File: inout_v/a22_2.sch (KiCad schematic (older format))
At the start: 38 parts, among them U2062 74HC02, U22028 74LVC07, U22029 74HC02, U22030 74HC27, U22032 74HC02, U22033 74HC27, U22034 74HC02, U22035 74HC4002, U22036 74HC02, U22037 74HC27, U22038 74HC02, U22039 74HC02, U22040 74HC02, U22041 74HC27, U22042 74HC02, U22043 74HC02, U22044 74HC27, U22045 74HC02, U22046 74HC4002, U22047 74HC02, U22048 74HC27, U22049 74HC02, U22050 74HC02, U22051 74HC27, U22052 74HC02, U22053 74HC02, U22054 74HC02, U22055 74HC27, U22056 74HC4002, U22057 74LVC07, U22058 74HC02, U22059 74HC02, U22060 74HC27, U22061 74HC02, U22062 74HC02, U22063 74HC27, U22064 74HC02, U22065 74HC02

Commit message: Added and tied in Inout VI. Pulled in all PIPA related things. Almost there!
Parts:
- added unit 3 of U22057
- added unit 2 of U22065
- added unit 3 of U22065
- added unit 4 of U22065
- added U22066: 74HC27, symbol 74HC27
- added U22067: 74HC02, symbol 74HC02
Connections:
- net CCH35: now also U22065.12, U22067.9
- net CHWL01/: now also U22065.6
- net DATA/: now also U22057.6
- net GND: now also U22057.7 (GND), U22065.7 (GND), U22065.7 (GND), U22065.7 (GND), U22066.7 (GND), U22066.7 (GND), U22067.7 (GND), U22067.7 (GND), U22067.7 (GND), U22067.7 (GND)
- net HIGH3/: now also U22066.1, U22066.3
- net LOW6/: now also U22066.13
- net LOW7/: now also U22066.5
- net PC15/: now also U22067.3
- net VCC: now also U22057.14 (VCC), U22065.14 (VCC), U22065.14 (VCC), U22065.14 (VCC), U22066.14 (VCC), U22066.14 (VCC), U22067.14 (VCC), U22067.14 (VCC), U22067.14 (VCC), U22067.14 (VCC)
- net WCH35/: now also U22065.5, U22067.2
- new net: U22065.4, U22065.8
- new net: U22065.10, U22065.11, U22066.2
- new net: U22065.13, U22065.9
- new net: U22066.12, U22067.11
- new net: U22067.1, U22067.5
- new net: U22066.4, U22067.4, U22067.8
- new net: U22067.10, U22067.6
- new net: U22066.6, U22067.12
- new net: U22057.5, U22067.13
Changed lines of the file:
@@
 Connection ~ 14650 1800
 Wire Wire Line
-	12850 2750 12850 18350
+	12850 2750 12850 20750
 Connection ~ 12850 2750
 Wire Wire Line
-	11550 1750 11550 17350
+	11550 1750 11550 19750
 Wire Wire Line
 	11550 2950 11600 2950
@@
 $EndComp
 Wire Wire Line
-	18300 3200 18300 12800
+	18300 3200 18300 18850
 $Comp
 L 74HC02 U22058
@@
 	14650 1800 14650 10200
 Wire Wire Line
-	14650 11400 14650 17400
+	14650 11400 14650 19800
 Wire Wire Line
 	18300 8000 18500 8000
@@
 Text HLabel 14600 11400 0    60   Input ~ 0
 HIGH3/
+Wire Wire Line
+	15900 18750 16200 18750
+Wire Wire Line
+	15900 19950 16100 19950
+$Comp
+L 74HC02 U22065
+U 2 1 574071CE
+P 12200 18650
+F 0 "U22065" H 12200 18700 60  0000 C CNN
+F 1 "74HC02" H 12250 18600 60  0000 C CNN
+F 2 "" H 12200 18650 60  0000 C CNN
+F 3 "" H 12200 18650 60  0000 C CNN
+	2    12200 18650
+	1    0    0    -1
+$EndComp
+$Comp
+L 74HC02 U22065
+U 3 1 574071D5
+P 13550 18750
+F 0 "U22065" H 13550 18800 60  0000 C CNN
+F 1 "74HC02" H 13600 18700 60  0000 C CNN
+F 2 "" H 13550 18750 60  0000 C CNN
+F 3 "" H 13550 18750 60  0000 C CNN
+F 4 "1" H 13800 18750 60  0000 C CIN "Initial"
+	3    13550 18750
+	1    0    0    -1
+$EndComp
+Wire Wire Line
+	12800 18650 12950 18650
+$Comp
+L 74HC02 U22065
+U 4 1 574071DC
+P 13550 19450
+F 0 "U22065" H 13550 19500 60  0000 C CNN
+F 1 "74HC02" H 13600 19400 60  0000 C CNN
+F 2 "" H 13550 19450 60  0000 C CNN
+F 3 "" H 13550 19450 60  0000 C CNN
+	4    13550 19450
+	1    0    0    -1
+$EndComp
+Wire Wire Line
+	14150 19450 14150 19200
+Wire Wire Line
+	14150 19200 12950 19000
+Wire Wire Line
+	12950 19000 12950 18850
+Wire Wire Line
+	14150 18750 14150 19000
+Wire Wire Line
+	14150 19000 12950 19200
+Wire Wire Line
+	12950 19200 12950 19350
+Wire Wire Line
+	12850 19550 12950 19550
+Connection ~ 14150 18750
+Wire Wire Line
+	14150 18750 14700 18750
+$Comp
+L 74HC27 U22066
+U 1 1 574071EB
+P 15300 18750
+F 0 "U22066" H 15300 18800 60  0000 C CNN
+F 1 "74HC27" H 15300 18700 60  0000 C CNN
+F 2 "" H 15300 18750 60  0000 C CNN
+F 3 "" H 15300 18750 60  0000 C CNN
+	1    15300 18750
+	1    0    0    -1
+$EndComp
+Wire Wire Line
+	14650 18600 14700 18600
+Wire Wire Line
+	14700 18900 14600 18900
+Text HLabel 14600 18900 0    60   Input ~ 0
+LOW6/
+Wire Wire Line
+	11550 18550 11600 18550
+Wire Wire Line
+	11600 18750 11500 18750
+Text HLabel 11500 18750 0    60   Input ~ 0
+CHWL01/
+$Comp
+L 74HC02 U22067
+U 1 1 574071F7
+P 12200 19850
+F 0 "U22067" H 12200 19900 60  0000 C CNN
+F 1 "74HC02" H 12250 19800 60  0000 C CNN
+F 2 "" H 12200 19850 60  0000 C CNN
+F 3 "" H 12200 19850 60  0000 C CNN
+	1    12200 19850
+	1    0    0    -1
+$EndComp
+$Comp
+L 74HC02 U22067
+U 2 1 574071FE
+P 13550 19950
+F 0 "U22067" H 13550 20000 60  0000 C CNN
+F 1 "74HC02" H 13600 19900 60  0000 C CNN
+F 2 "" H 13550 19950 60  0000 C CNN
+F 3 "" H 13550 19950 60  0000 C CNN
+F 4 "1" H 13800 19950 60  0000 C CIN "Initial"
+	2    13550 19950
+	1    0    0    -1
+$EndComp
+Wire Wire Line
+	12800 19850 12950 19850
+$Comp
+L 74HC02 U22067
+U 3 1 57407205
+P 13550 20650
+F 0 "U22067" H 13550 20700 60  0000 C CNN
+F 1 "74HC02" H 13600 20600 60  0000 C CNN
+F 2 "" H 13550 20650 60  0000 C CNN
+F 3 "" H 13550 20650 60  0000 C CNN
+	3    13550 20650
+	1    0    0    -1
+$EndComp
+Wire Wire Line
+	14150 20650 14150 20400
+Wire Wire Line
+	14150 20400 12950 20200
+Wire Wire Line
+	12950 20200 12950 20050
+Wire Wire Line
+	14150 19950 14150 20200
+Wire Wire Line
+	14150 20200 12950 20400
+Wire Wire Line
+	12950 20400 12950 20550
+Wire Wire Line
+	12850 20750 12950 20750
+Connection ~ 14150 19950
+Wire Wire Line
+	14150 19950 14700 19950
+$Comp
+L 74HC27 U22066
+U 2 1 57407214
+P 15300 19950
+F 0 "U22066" H 15300 20000 60  0000 C CNN
+F 1 "74HC27" H 15300 19900 60  0000 C CNN
+F 2 "" H 15300 19950 60  0000 C CNN
+F 3 "" H 15300 19950 60  0000 C CNN
+	2    15300 19950
+	1    0    0    -1
+$EndComp
+Wire Wire Line
+	14650 19800 14700 19800
+Wire Wire Line
+	14700 20100 14600 20100
+Text HLabel 14600 20100 0    60   Input ~ 0
+LOW7/
+Wire Wire Line
+	11550 19750 11600 19750
+Wire Wire Line
+	11600 19950 11500 19950
+Text HLabel 11500 19950 0    60   Input ~ 0
+PC15/
+Connection ~ 14650 18600
+Connection ~ 12850 19550
+Connection ~ 11550 18550
+Connection ~ 14650 17400
+Connection ~ 11550 17350
+Connection ~ 12850 18350
+$Comp
+L 74LVC07 U22057
+U 3 1 574121D2
+P 17850 18850
+F 0 "U22057" H 18045 18965 60  0000 C CNN
+F 1 "74LVC07" H 18040 18725 60  0000 C CNN
+F 2 "" H 17850 18850 60  0000 C CNN
+F 3 "" H 17850 18850 60  0000 C CNN
+	3    17850 18850
+	1    0    0    -1
+$EndComp
+$Comp
+L 74HC02 U22067
+U 4 1 574123F8
+P 16800 18850
+F 0 "U22067" H 16800 18900 60  0000 C CNN
+F 1 "74HC02" H 16850 18800 60  0000 C CNN
+F 2 "" H 16800 18850 60  0000 C CNN
+F 3 "" H 16800 18850 60  0000 C CNN
+	4    16800 18850
+	1    0    0    -1
+$EndComp
+Wire Wire Line
+	16100 19950 16100 18950
+Wire Wire Line
+	16100 18950 16200 18950
+Connection ~ 18300 12800
 $EndSCHEMATC

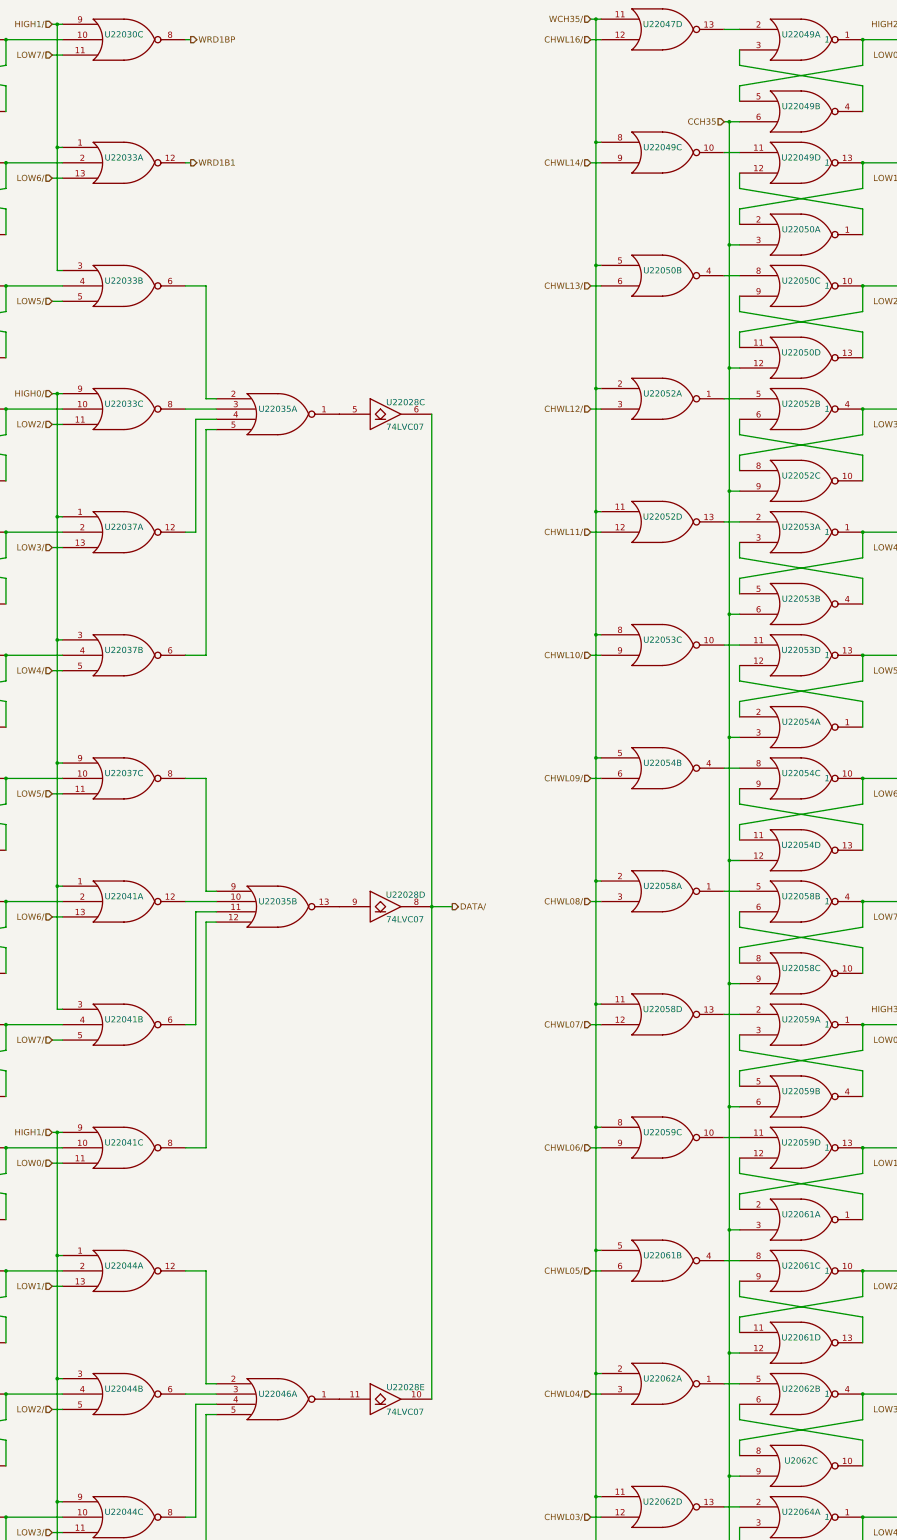
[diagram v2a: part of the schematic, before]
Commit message: Power net updates for Counter Cell I+II and Inout V
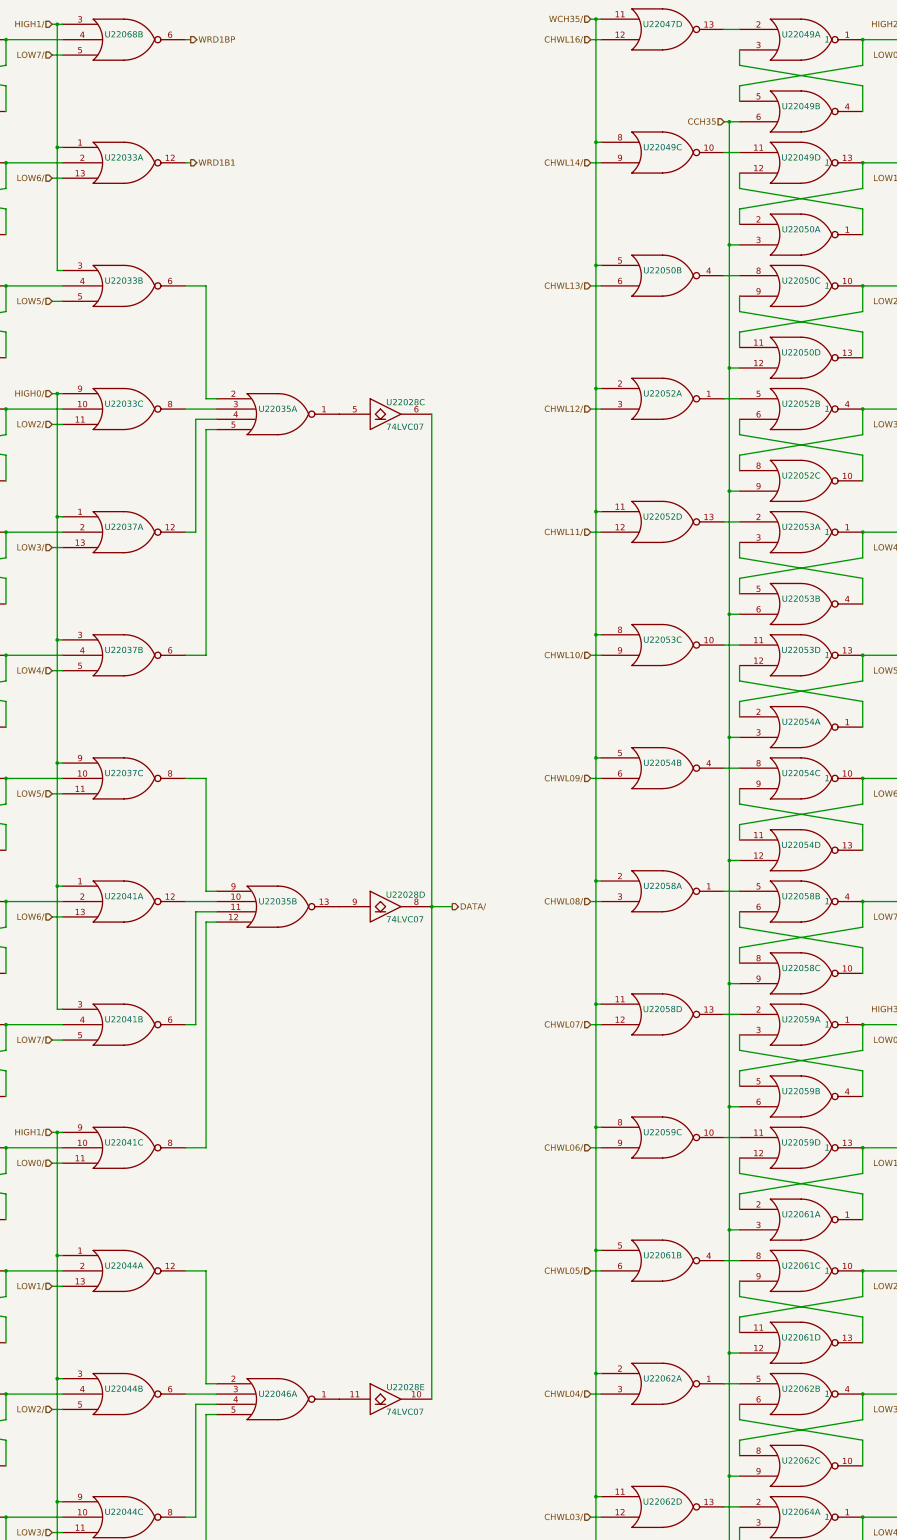
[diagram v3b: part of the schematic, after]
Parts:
- renumbered U2062 to U22062, U22030 to U22068
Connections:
- net HIGH1/: now also U22068.3; no longer U22068.9
- net LOW7/: now also U22068.5; no longer U22068.11
- net WRD1BP: now also U22068.6; no longer U22068.8
- net at U22029.10, U22029.11: now also U22068.4; no longer U22068.10
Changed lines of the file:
@@
 	5800 1950 6350 1950
 $Comp
-L 74HC27 U22030
-U 3 1 57304DEF
+L 74HC27 U22068
+U 2 1 57304DEF
 P 6950 1950
-F 0 "U22030" H 6950 2000 60  0000 C CNN
+F 0 "U22068" H 6950 2000 60  0000 C CNN
 F 1 "74HC27" H 6950 1900 60  0001 C CNN
 F 2 "" H 6950 1950 60  0000 C CNN
 F 3 "" H 6950 1950 60  0000 C CNN
-	3    6950 1950
+	2    6950 1950
 	1    0    0    -1
 $EndComp
@@
 	12800 15050 12950 15050
 $Comp
-L 74HC02 U2062
+L 74HC02 U22062
 U 3 1 57328CE1
 P 13550 15850
-F 0 "U2062" H 13550 15900 60  0000 C CNN
+F 0 "U22062" H 13550 15900 60  0000 C CNN
 F 1 "74HC02" H 13600 15800 60  0001 C CNN
 F 2 "" H 13550 15850 60  0000 C CNN
